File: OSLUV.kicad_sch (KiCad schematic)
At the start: 1 part

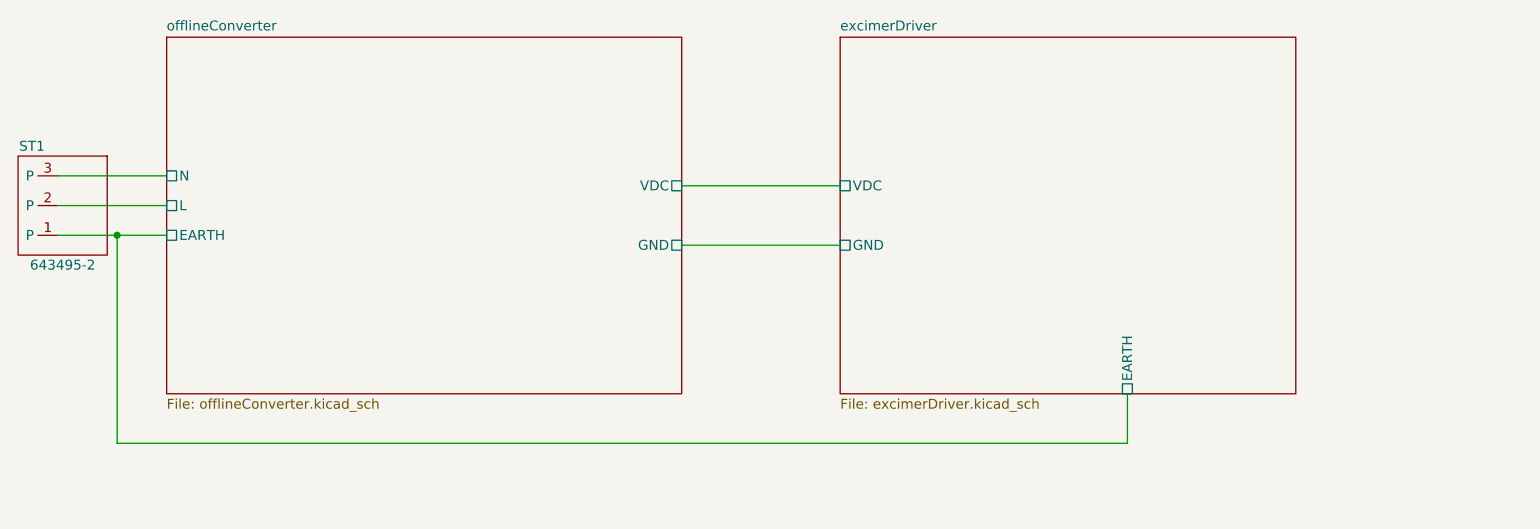
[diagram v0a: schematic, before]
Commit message: update of schematic
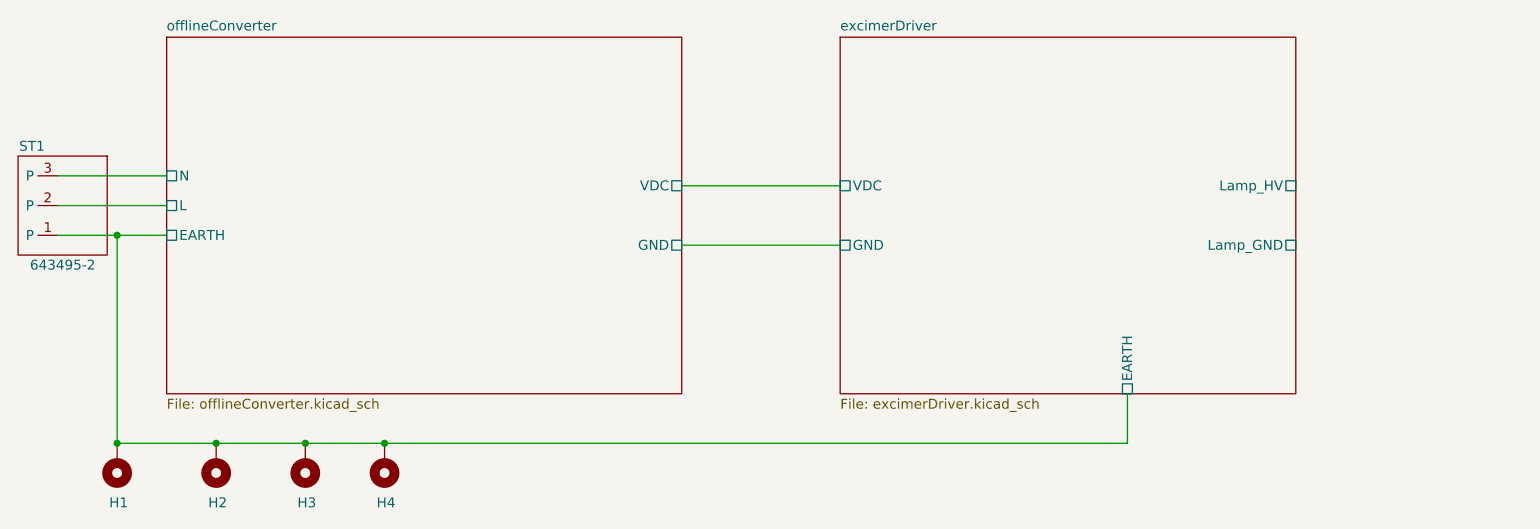
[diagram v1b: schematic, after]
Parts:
- added H1, H2, H3, H4: MountingHole_Pad, Hansmann:Mounting_M3_NPTH_Vias, symbol Mechanical:MountingHole_Pad
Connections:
- net excimerDriver/EARTH: now also H1.1, H2.1, H3.1, H4.1
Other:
- sheet excimerDriver ports: added Lamp_GND, Lamp_HV; removed none

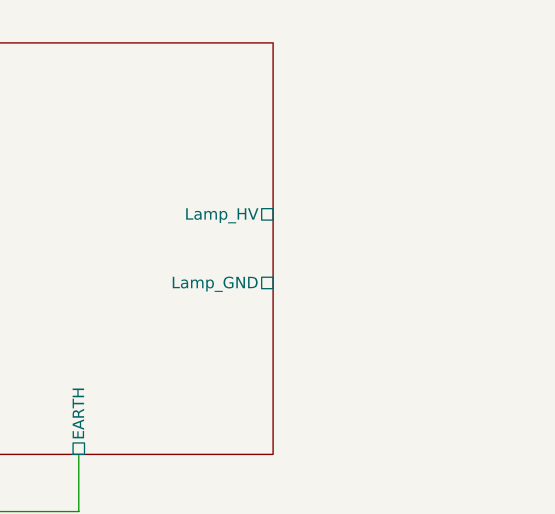
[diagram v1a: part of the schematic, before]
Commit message: schematic done, not placed
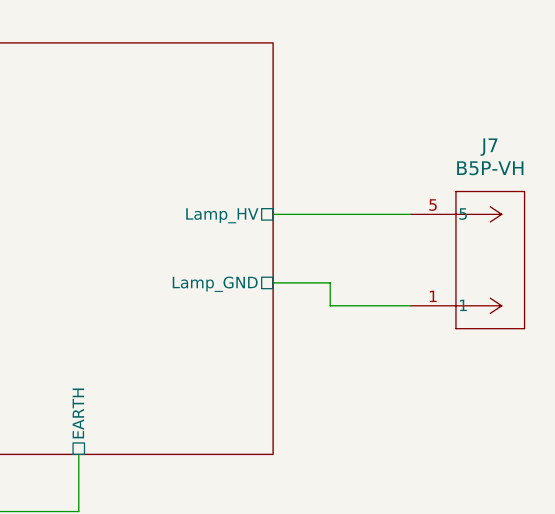
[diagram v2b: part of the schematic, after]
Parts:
- added J7: B5P-VH, Hansmann:CONN_B2P5-VH_JST, symbol Hansmann:B2P5-VH
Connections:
- net excimerDriver/Lamp_GND: now also J7.1
- net excimerDriver/Lamp_HV: now also J7.5
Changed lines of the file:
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@@
+	(wire
+		(pts
+			(xy 229.87 96.52) (xy 238.76 96.52)
+		)
+		(stroke
+			(width 0)
+			(type default)
+		)
+	)
 	(wire
 		(pts
@@
 	(wire
 		(pts
+			(xy 223.52 86.36) (xy 238.76 86.36)
+		)
+		(stroke
+			(width 0)
+			(type default)
+		)
+	)
+	(wire
+		(pts
 			(xy 72.39 119.38) (xy 72.39 92.71)
 		)
@@
 		(pts
 			(xy 201.93 113.03) (xy 201.93 119.38)
+		)
+		(stroke
+			(width 0)
+			(type default)
+		)
+	)
+	(wire
+		(pts
+			(xy 223.52 93.98) (xy 229.87 93.98)
+		)
+		(stroke
+			(width 0)
+			(type default)
+		)
+	)
+	(wire
+		(pts
+			(xy 229.87 93.98) (xy 229.87 96.52)
 		)
 		(stroke
@@
 					(unit 1)
 				)
+			)
+		)
+	)
+	(symbol
+		(lib_id "Hansmann:B2P5-VH")
+		(at 238.76 96.52 0)
+		(mirror x)
+		(unit 1)
+		(exclude_from_sim no)
+		(in_bom yes)
+		(on_board yes)
+		(dnp no)
+		(fields_autoplaced yes)
+		(property "Reference" "J7"
+			(at 247.65 78.74 0)
+			(effects
+				(font
+					(size 1.524 1.524)
+				)
+			)
+		)
+		(property "Value" "B5P-VH"
+			(at 247.65 81.28 0)
+			(effects
+				(font
+					(size 1.524 1.524)
+				)
+			)
+		)
+		(property "Footprint" "Hansmann:CONN_B2P5-VH_JST"
+			(at 238.76 96.52 0)
+			(effects
+				(font
+					(size 1.27 1.27)
+					(italic yes)
+				)
+				(hide yes)
+			)
+		)
+		(property "Datasheet" "B5P-VH"
+			(at 238.76 96.52 0)
+			(effects
+				(font
+					(size 1.27 1.27)
+					(italic yes)
+				)
+				(hide yes)
+			)
+		)
+		(property "Description" ""
+			(at 238.76 96.52 0)
+			(effects
+				(font
+					(size 1.27 1.27)
+				)
+				(hide yes)
+			)
+		)
+		(pin "1"
+		)
+		(pin "5"
+		)
+		(instances
+			(project ""
+				(path "/c6e900e0-9399-44f0-8089-9dd7b8ffe54c"
+					(reference "J7")
+					(unit 1)
+				)

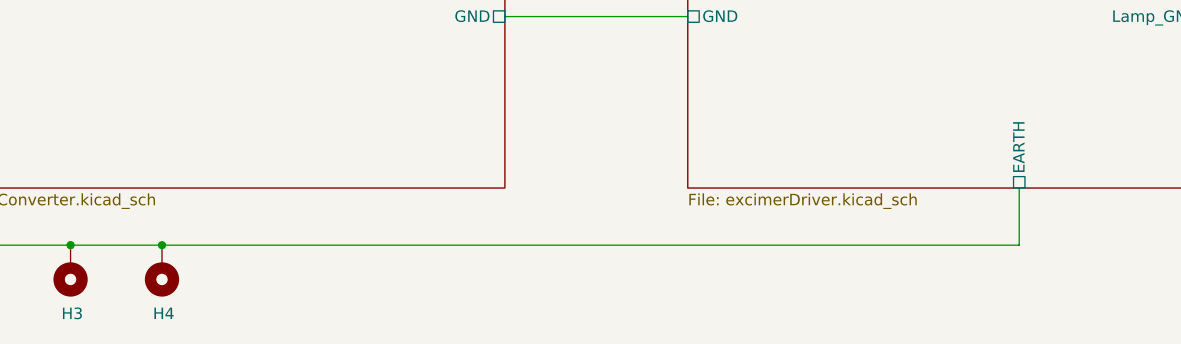
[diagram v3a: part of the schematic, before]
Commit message: branch main, transfomer changed to EF25
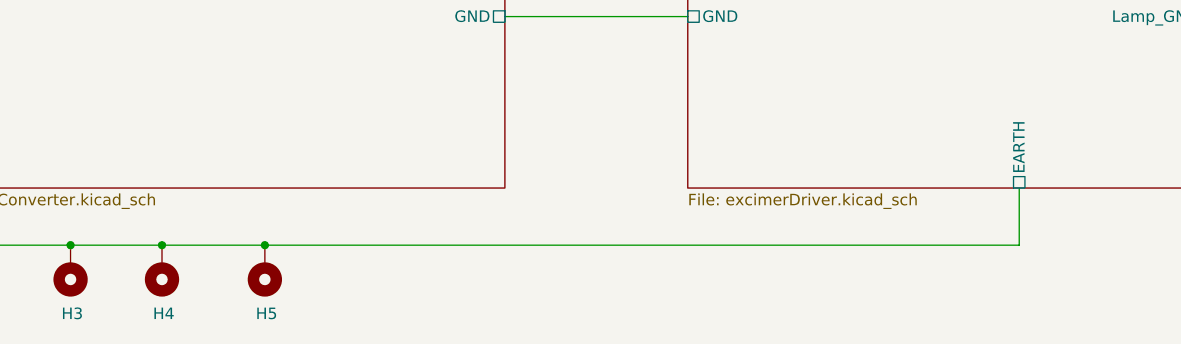
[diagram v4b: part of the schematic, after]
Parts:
- added H5: MountingHole_Pad, Hansmann:Mounting_M3_NPTH_Vias, symbol Mechanical:MountingHole_Pad
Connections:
- net excimerDriver/EARTH: now also H5.1
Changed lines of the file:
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@@
 	(paper "A4")
 	(junction
+		(at 118.11 119.38)
+		(diameter 0)
+		(color 0 0 0 0)
+	)
+	(junction
 		(at 106.68 119.38)
 		(diameter 0)
@@
 	(wire
 		(pts
+			(xy 118.11 119.38) (xy 201.93 119.38)
+		)
+		(stroke
+			(width 0)
+			(type default)
+		)
+	)
+	(wire
+		(pts
 			(xy 223.52 93.98) (xy 229.87 93.98)
 		)
@@
 	(wire
 		(pts
-			(xy 106.68 119.38) (xy 201.93 119.38)
+			(xy 106.68 119.38) (xy 118.11 119.38)
 		)
 		(stroke
@@
 					(unit 1)
 				)
+			)
+		)
+	)
+	(symbol
+		(lib_id "Mechanical:MountingHole_Pad")
+		(at 118.11 121.92 180)
+		(unit 1)
+		(exclude_from_sim no)
+		(in_bom no)
+		(on_board yes)
+		(dnp no)
+		(property "Reference" "H5"
+			(at 117.094 127 0)
+			(effects
+				(font
+					(size 1.27 1.27)
+				)
+				(justify right)
+			)
+		)
+		(property "Value" "MountingHole_Pad"
+			(at 110.744 127 0)
+			(hide yes)
+			(effects
+				(font
+					(size 1.27 1.27)
+				)
+				(justify right)
+			)
+		)
+		(property "Footprint" "Hansmann:Mounting_M3_NPTH_Vias"
+			(at 118.11 121.92 0)
+			(hide yes)
+			(effects
+				(font
+					(size 1.27 1.27)
+				)
+			)
+		)
+		(property "Datasheet" ""
+			(at 118.11 121.92 0)
+			(hide yes)
+			(effects
+				(font
+					(size 1.27 1.27)
+				)
+			)
+		)
+		(property "Description" "Mounting Hole with connection"
+			(at 118.11 121.92 0)
+			(hide yes)
+			(effects
+				(font
+					(size 1.27 1.27)
+				)
+			)
+		)
+		(pin "1"
+		)
+		(instances
+			(project "OSLUV"
+				(path "/c6e900e0-9399-44f0-8089-9dd7b8ffe54c"
+					(reference "H5")
+					(unit 1)
+				)
